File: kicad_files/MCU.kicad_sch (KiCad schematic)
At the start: 31 parts, among them SW1 SW_Push, SW2 SW_Push, U1 STM32F407ZGTx, Y1 LFXTAL036869Reel 8MHz Crystal

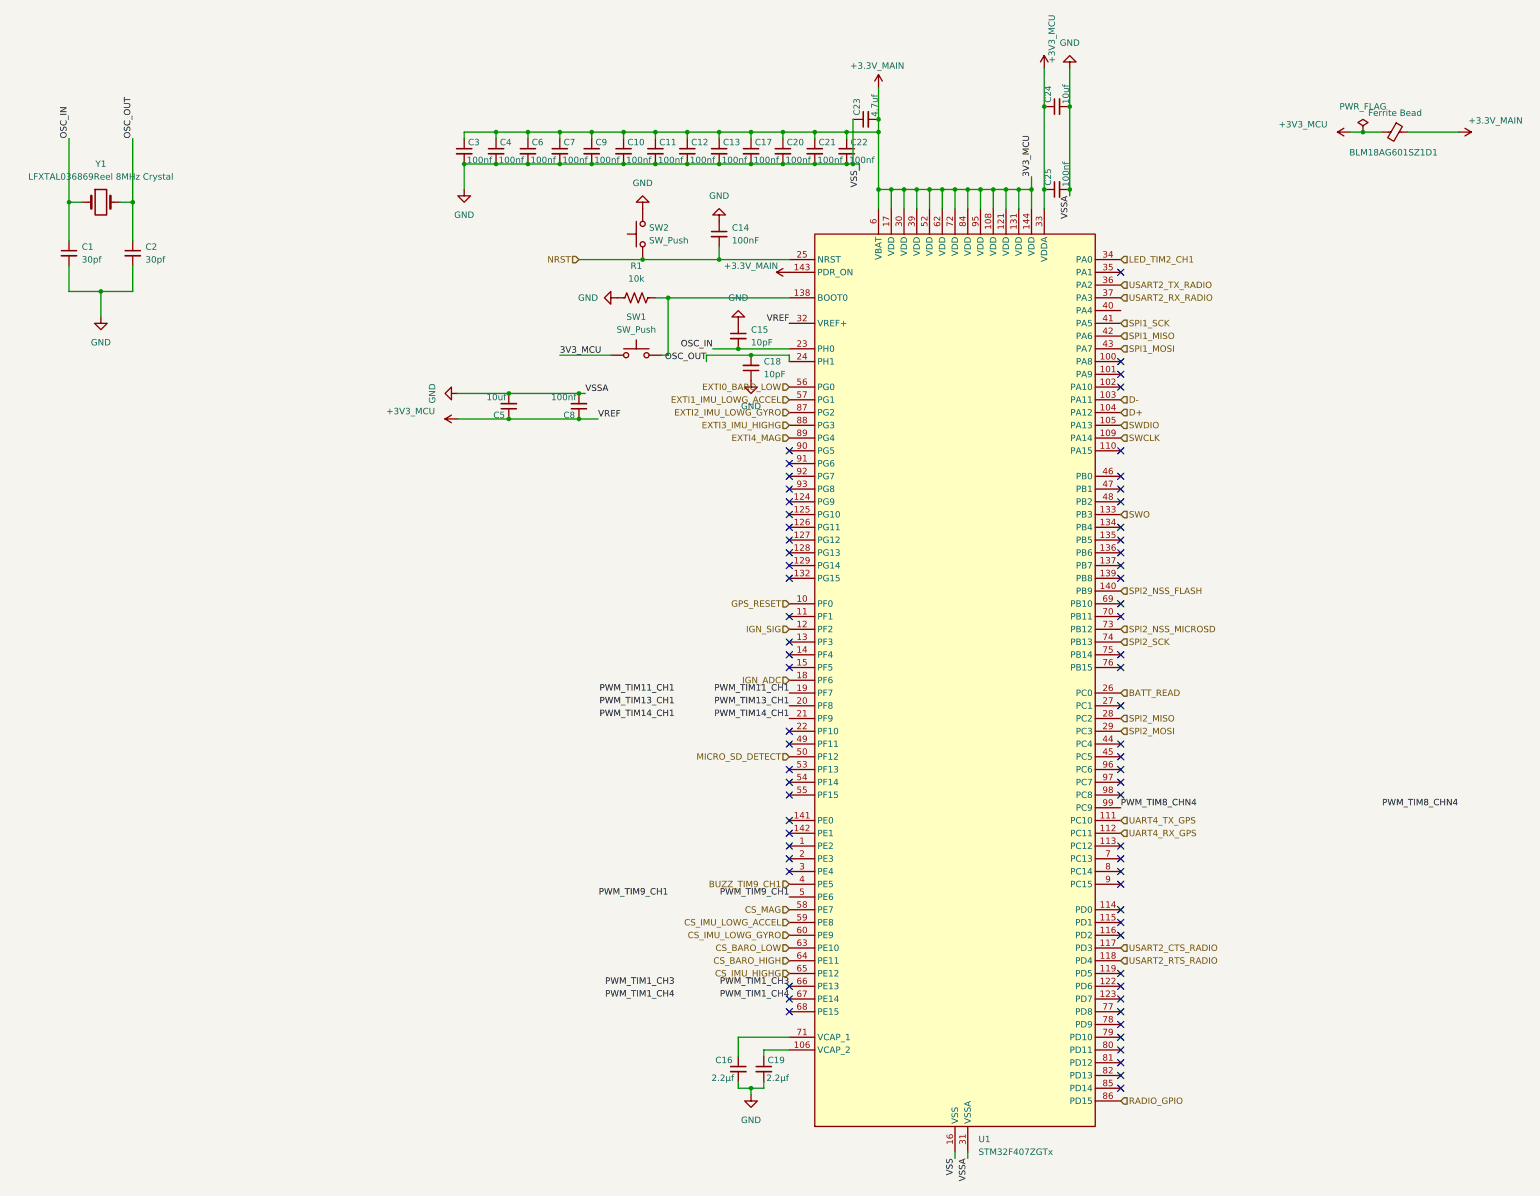
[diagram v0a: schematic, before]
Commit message: add gitignore, rm extra git repo, switch mcu
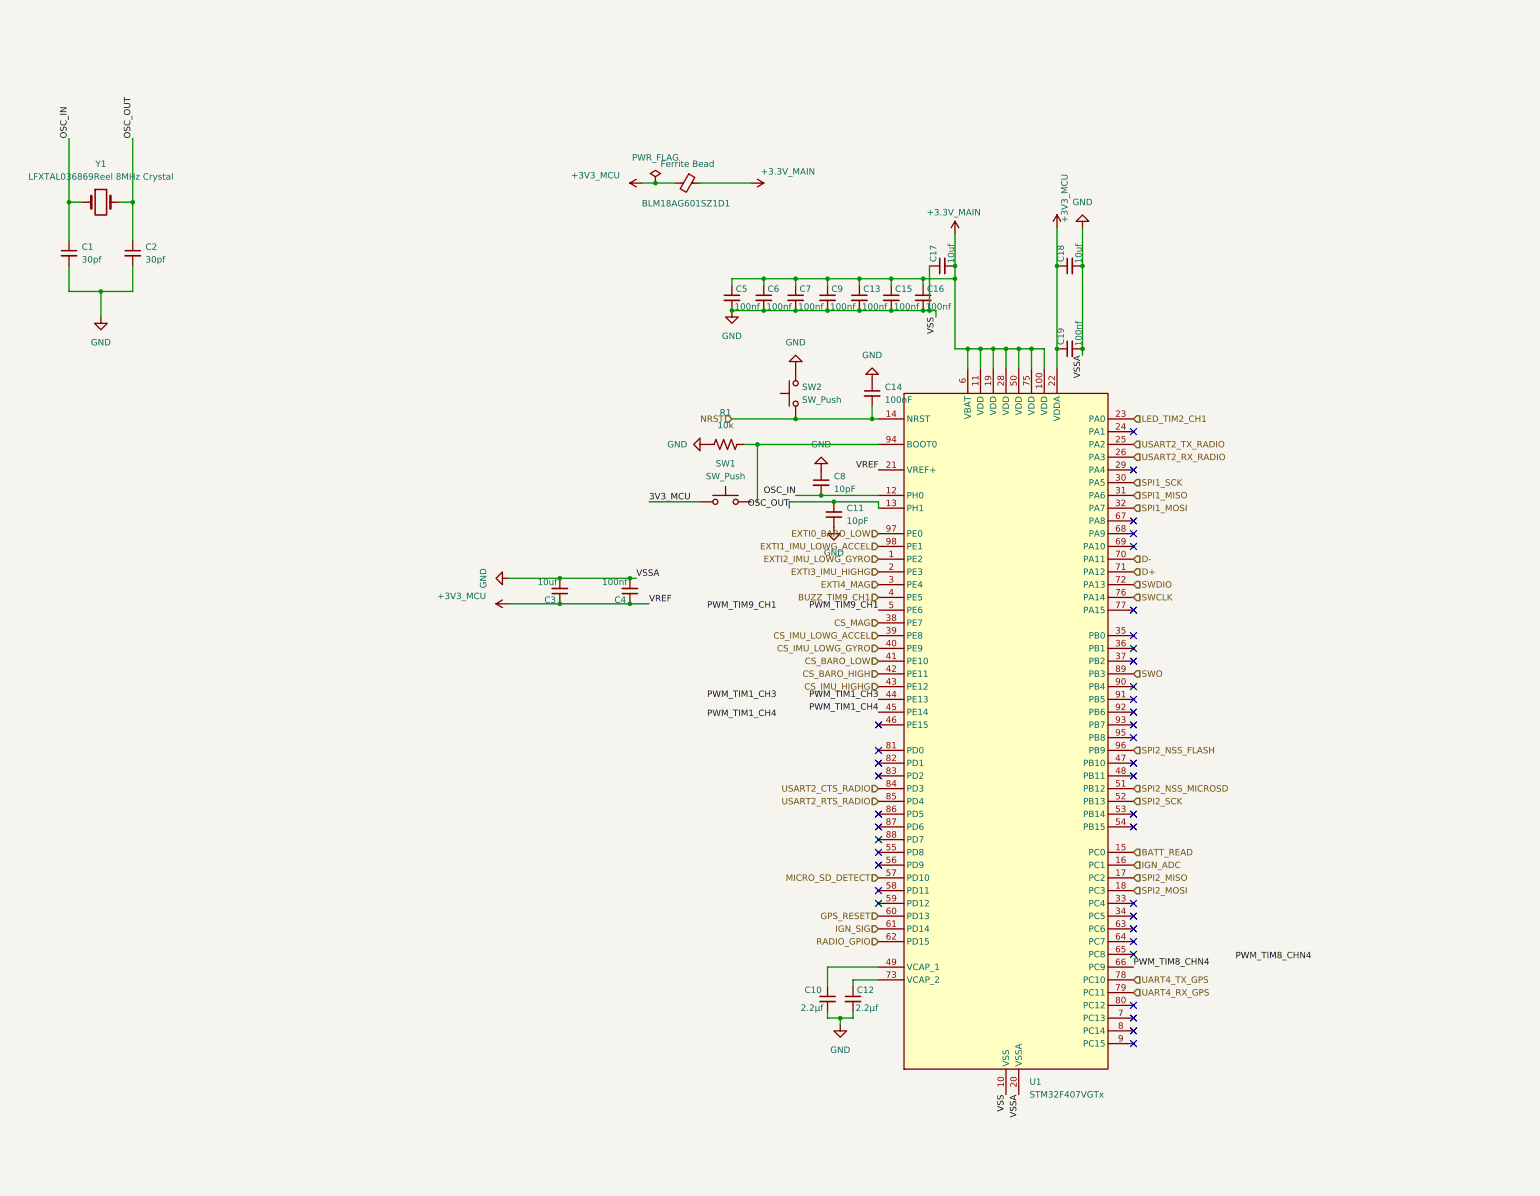
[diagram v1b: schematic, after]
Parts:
- removed C20, C21, C22, C25, C3, C4: 100nf, Capacitor_SMD:C_0402_1005Metric, symbol Device:C_Small
- removed C23: 4.7uf, Capacitor_SMD:C_0603_1608Metric, symbol Device:C_Small
- removed C24: 10uf, Capacitor_SMD:C_0805_2012Metric, symbol Device:C_Small
- removed U1: STM32F407ZGTx, Package_QFP:LQFP-144_20x20mm_P0.5mm, symbol MCU_ST_STM32F4:STM32F407ZGTx
- added C5: 100nf, Capacitor_SMD:C_0402_1005Metric, symbol Device:C_Small
- added C8: 10pF, Capacitor_SMD:C_0402_1005Metric, symbol Device:C_Small
- added U1: STM32F407VGTx, Package_QFP:LQFP-100_14x14mm_P0.5mm, symbol MCU_ST_STM32F4:STM32F407VGTx
- C10, C12: value 100nf -> 2.2µf; footprint Capacitor_SMD:C_0402_1005Metric -> Capacitor_SMD:C_0603_1608Metric
- C11: value 100nf -> 10pF
- C15: value 10pF -> 100nf
- C16, C19: value 2.2µf -> 100nf; footprint Capacitor_SMD:C_0603_1608Metric -> Capacitor_SMD:C_0402_1005Metric
- C17: value 100nf -> 10uf; footprint Capacitor_SMD:C_0402_1005Metric -> Capacitor_SMD:C_0603_1608Metric
- C18: value 10pF -> 10uf; footprint Capacitor_SMD:C_0402_1005Metric -> Capacitor_SMD:C_0805_2012Metric
- renumbered C5 to C3, C8 to C4
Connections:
- net +3.3V_MAIN: now also C15.1, C16.1, C17.2, C5.1, U1.100 (VDD), U1.11 (VDD), U1.19 (VDD), U1.28 (VDD), U1.50 (VDD), U1.6 (VBAT), U1.75 (VDD); no longer C10.1, C11.1, C12.1, C17.1, SW1.1
- net +3V3_MCU: now also C18.1, C19.1, U1.21 (VREF+), U1.22 (VDDA)
- net BATT_READ: now also U1.15 (PC0)
- net BUZZ_TIM9_CH1: now also U1.4 (PE5)
- net CS_BARO_HIGH: now also U1.42 (PE11)
- net CS_BARO_LOW: now also U1.41 (PE10)
- net CS_IMU_HIGHG: now also U1.43 (PE12)
- net CS_IMU_LOWG_ACCEL: now also U1.39 (PE8)
- net CS_IMU_LOWG_GYRO: now also U1.40 (PE9)
- net CS_MAG: now also U1.38 (PE7)
- net D+: now also U1.71 (PA12)
- net D-: now also U1.70 (PA11)
- net EXTI0_BARO_LOW: now also U1.97 (PE0)
- net EXTI1_IMU_LOWG_ACCEL: now also U1.98 (PE1)
- net EXTI2_IMU_LOWG_GYRO: now also U1.1 (PE2)
- net EXTI3_IMU_HIGHG: now also U1.2 (PE3)
- net EXTI4_MAG: now also U1.3 (PE4)
- net GND: now also C11.1, C15.2, C17.1, C18.2, C5.2, C8.1, U1.10 (VSS), U1.20 (VSSA), U1.27 (VSS), U1.74 (VSS), U1.99 (VSS); no longer C11.2, C15.1, C17.2, C18.1
- net GPS_RESET: now also U1.60 (PD13)
- net IGN_ADC: now also U1.16 (PC1)
- net IGN_SIG: now also U1.61 (PD14)
- net LED_TIM2_CH1: now also U1.23 (PA0)
- net MICRO_SD_DETECT: now also U1.57 (PD10)
- net NRST: now also U1.14 (NRST)
- net OSC_IN: now also C8.2, U1.12 (PH0); no longer C15.2
- net OSC_OUT: now also C11.2, U1.13 (PH1); no longer C18.2
- net PWM_TIM1_CH3: now also U1.44 (PE13)
- net PWM_TIM1_CH4: now also U1.45 (PE14)
- net PWM_TIM8_CHN4: now also U1.66 (PC9)
- net PWM_TIM9_CH1: now also U1.5 (PE6)
- net RADIO_GPIO: now also U1.62 (PD15)
- net SPI1_MISO: now also U1.31 (PA6)
- net SPI1_MOSI: now also U1.32 (PA7)
- net SPI1_SCK: now also U1.30 (PA5)
- net SPI2_MISO: now also U1.17 (PC2)
- net SPI2_MOSI: now also U1.18 (PC3)
- net SPI2_NSS_FLASH: now also U1.96 (PB9)
- net SPI2_NSS_MICROSD: now also U1.51 (PB12)
- net SPI2_SCK: now also U1.52 (PB13)
- net SWCLK: now also U1.76 (PA14)
- net SWDIO: now also U1.72 (PA13)
- net SWO: now also U1.89 (PB3)
- net UART4_RX_GPS: now also U1.79 (PC11)
- net UART4_TX_GPS: now also U1.78 (PC10)
- net USART2_CTS_RADIO: now also U1.84 (PD3)
- net USART2_RTS_RADIO: now also U1.85 (PD4)
- net USART2_RX_RADIO: now also U1.26 (PA3)
- net USART2_TX_RADIO: now also U1.25 (PA2)
- net at SW1.2: no longer R1.2
- new net: C10.1, U1.49 (VCAP_1)
- new net: C12.1, U1.73 (VCAP_2)
- new net: R1.2, U1.94 (BOOT0)
- new net 3V3_MCU: SW1.1
- no-connect marks 68 -> 38
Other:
- moved on the sheet: BLM18AG601SZ1D1, C3, C4

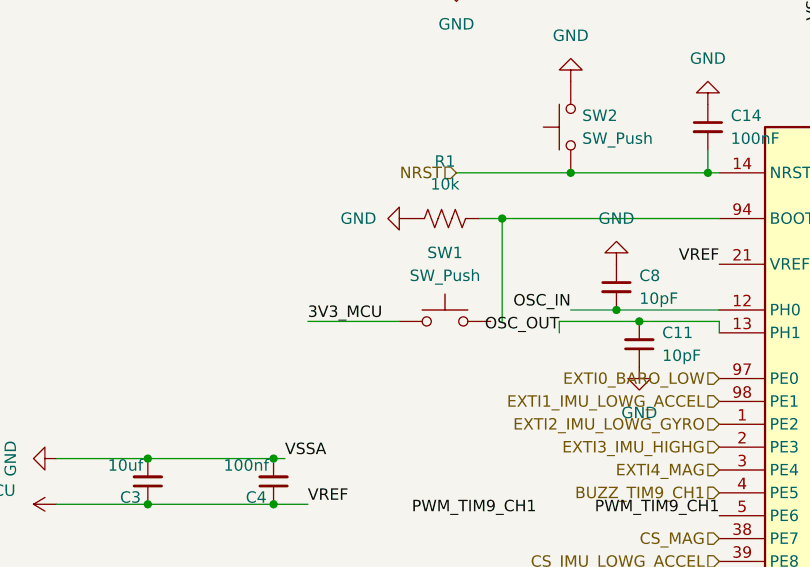
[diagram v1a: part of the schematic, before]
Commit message: Fix PCB conflict (pls work)
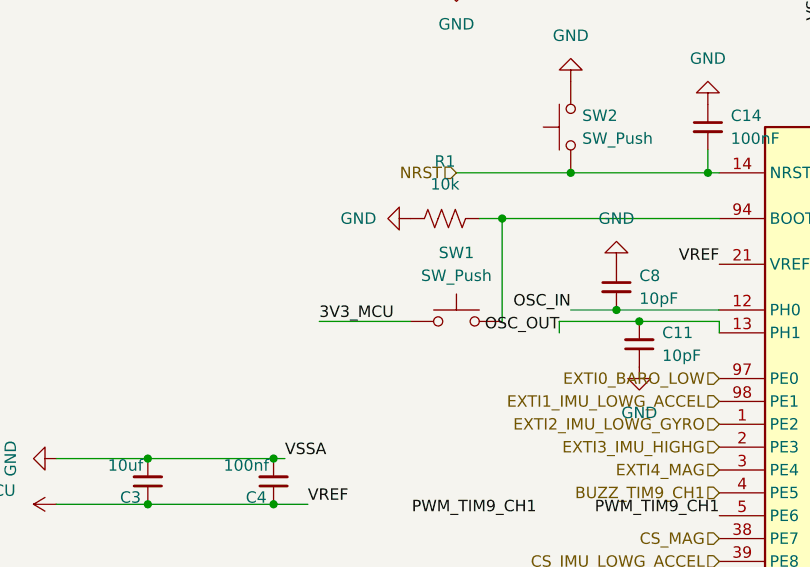
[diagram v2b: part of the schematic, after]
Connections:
- net at SW1.2: now also R1.2, U1.94 (BOOT0)
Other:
- moved on the sheet: SW1
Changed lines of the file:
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@@
 	(wire
 		(pts
-			(xy 153.67 110.49) (xy 163.83 110.49)
+			(xy 154.94 110.49) (xy 165.1 110.49)
 		)
 		(stroke
@@
 	)
 	(label "3V3_MCU"
-		(at 153.67 110.49 0)
+		(at 154.94 110.49 0)
 		(effects
 			(font
@@
 	(symbol
 		(lib_id "Switch:SW_Push")
-		(at 168.91 110.49 0)
+		(at 170.18 110.49 0)
 		(unit 1)
 		(body_style 1)
@@
 		(fields_autoplaced yes)
 		(property "Reference" "SW1"
-			(at 168.91 102.87 0)
+			(at 170.18 102.87 0)
 			(show_name no)
 			(do_not_autoplace no)
@@
 		)
 		(property "Value" "SW_Push"
-			(at 168.91 105.41 0)
+			(at 170.18 105.41 0)
 			(show_name no)
 			(do_not_autoplace no)
@@
 		)
 		(property "Footprint" "Button_Switch_SMD:SW_SPST_PTS810"
-			(at 168.91 105.41 0)
+			(at 170.18 105.41 0)
 			(hide yes)
 			(show_name no)
@@
 		)
 		(property "Datasheet" ""
-			(at 168.91 105.41 0)
+			(at 170.18 105.41 0)
 			(hide yes)
 			(show_name no)
@@
 		)
 		(property "Description" "Push button switch, generic, two pins"
-			(at 168.91 110.49 0)
-			(hide yes)
-			(show_name no)
+			(at 170.18 110.49 0)
+			(hide yes)
+			(show_name no)

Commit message: make schematic changes
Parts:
- C17: footprint Capacitor_SMD:C_0603_1608Metric -> Capacitor_SMD:C_0805_2012Metric
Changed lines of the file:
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@@
 			)
 		)
-		(property "Footprint" "Capacitor_SMD:C_0603_1608Metric"
+		(property "Footprint" "Capacitor_SMD:C_0805_2012Metric"
 			(at 212.09 63.5 0)
 			(hide yes)

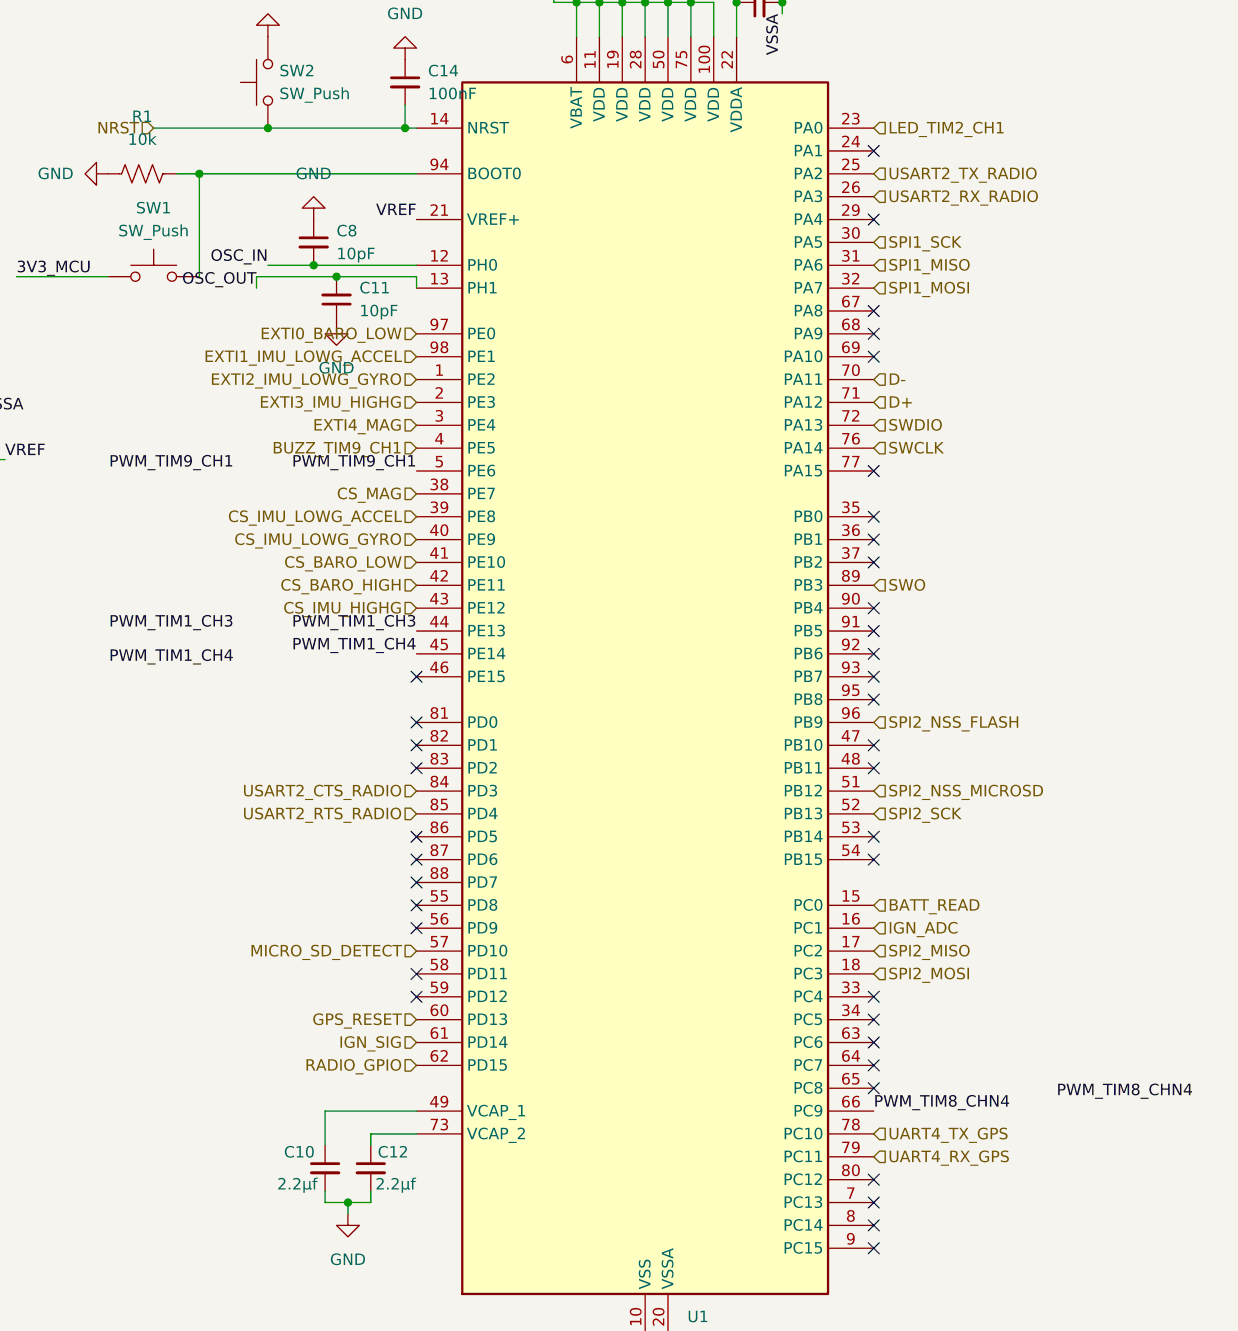
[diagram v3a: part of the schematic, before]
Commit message: switch uart, usart, spi lines, adc, pwm
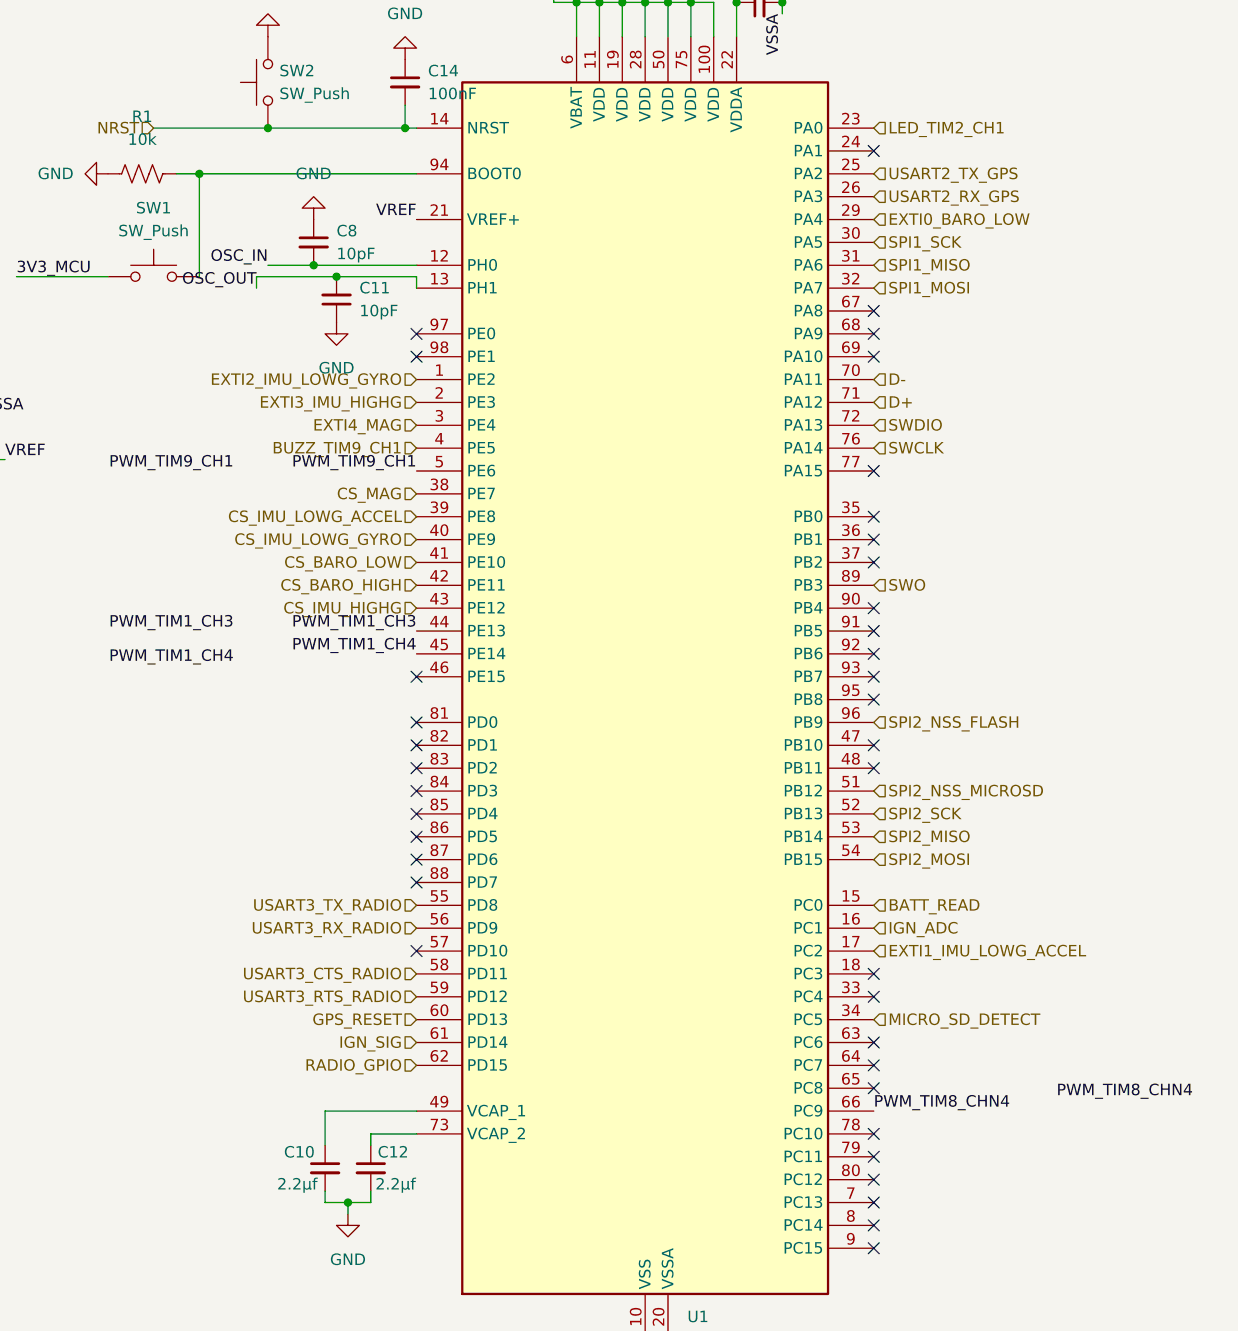
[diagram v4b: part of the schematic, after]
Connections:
- net EXTI0_BARO_LOW: now also U1.29 (PA4); no longer U1.97 (PE0)
- net EXTI1_IMU_LOWG_ACCEL: now also U1.17 (PC2); no longer U1.98 (PE1)
- net MICRO_SD_DETECT: now also U1.34 (PC5); no longer U1.57 (PD10)
- net SPI2_MISO: now also U1.53 (PB14); no longer U1.17 (PC2)
- net SPI2_MOSI: now also U1.54 (PB15); no longer U1.18 (PC3)
- net USART3_TX_RADIO: now reaches U1.55 (PD8)
- net USART3_RX_RADIO: now reaches U1.56 (PD9)
- net USART3_CTS_RADIO: now reaches U1.58 (PD11)
- net USART3_RTS_RADIO: now reaches U1.59 (PD12)
- net UART4_RX_GPS: no longer names the net of U1.79 (PC11)
- net UART4_TX_GPS: no longer names the net of U1.78 (PC10)
- net USART2_CTS_RADIO: no longer names the net of U1.84 (PD3)
- net USART2_RTS_RADIO: no longer names the net of U1.85 (PD4)
- net USART2_RX_RADIO renamed USART2_RX_GPS
- net USART2_TX_RADIO renamed USART2_TX_GPS
